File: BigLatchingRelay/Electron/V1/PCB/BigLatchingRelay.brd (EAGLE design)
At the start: 89.5 x 29.3 mm, 13 parts, among them IC2 BD6211F

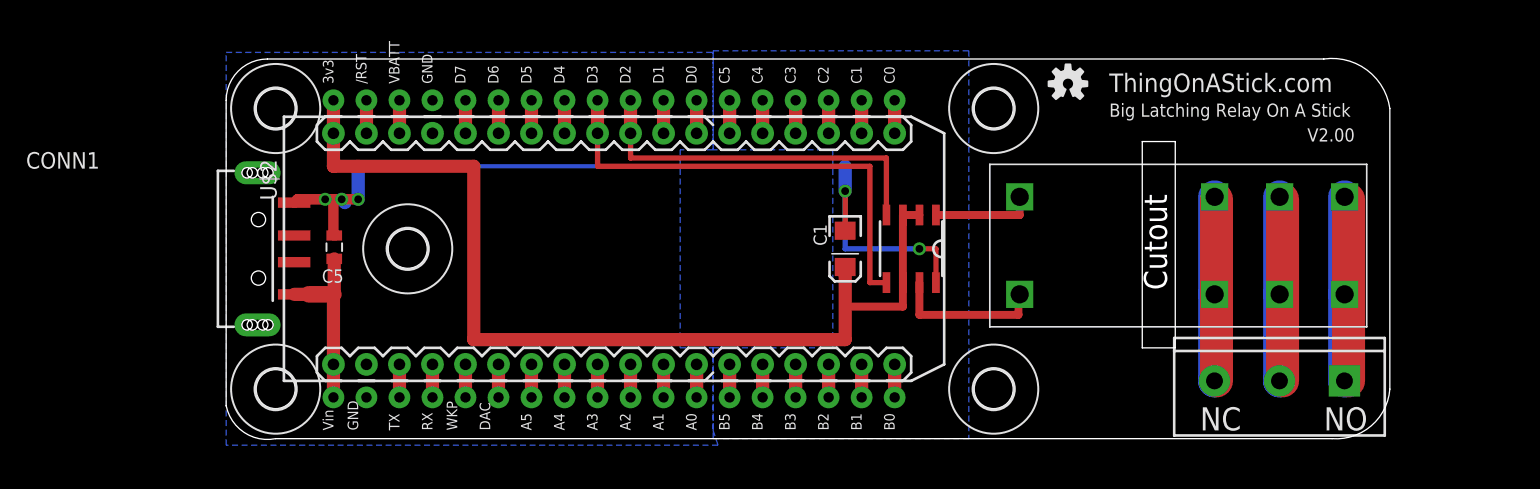
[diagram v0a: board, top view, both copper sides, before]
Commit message: Renamed BigLatchingRelay. Updated to V2.1: Moved connector to end rather than side to reduce strain on one side when USB A connector used. Added OSH Logo LED (and bigger OSH Logo). Added high volage warning text to board top and bottom. Added PDFs of board and schematic.
Added DirtyPcb images.
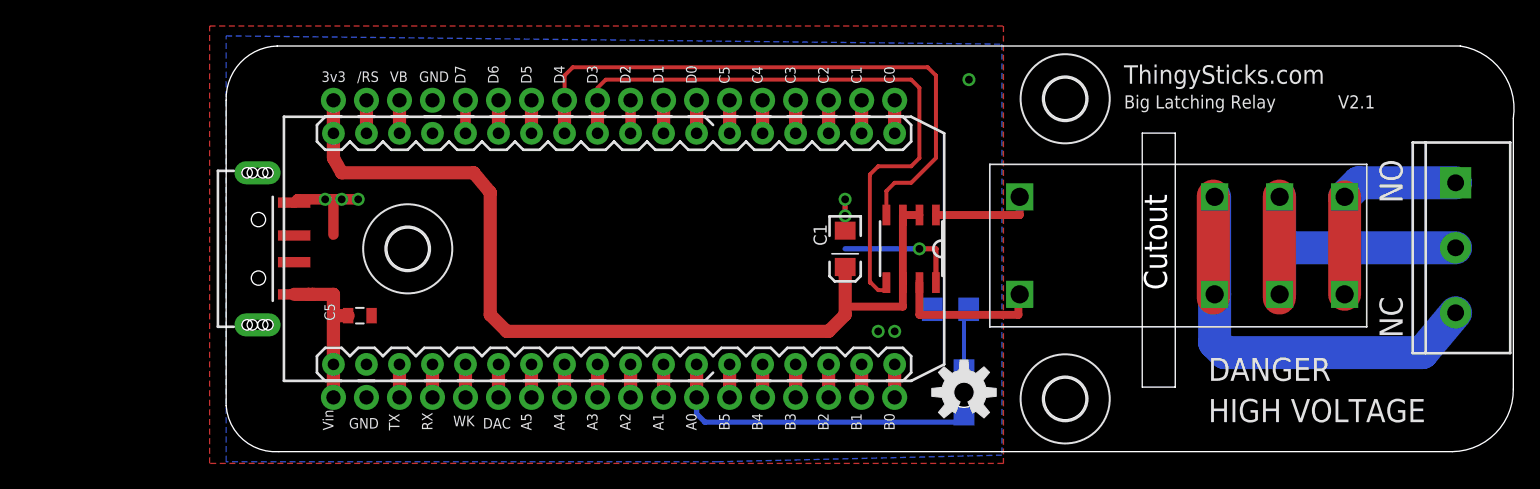
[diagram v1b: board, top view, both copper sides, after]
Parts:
- removed H4, H5: MOUNT-HOLE3.0, holes:3,0
- removed LOGO2: OSHW-LOGOS, SparkFun-Aesthetics:OSHW-LOGO-S
- added D1: (no value), SparkFun-LED:LED-1206-BOTTOM
- added LOGO1: OSHW-LOGOM, SparkFun-Aesthetics:OSHW-LOGO-M
- added R1: (no value), SparkFun-Resistors:1206
- H1, H2, H3: value MOUNT-HOLE3.0 -> MOUNT-HOLE3.2; device holes:3,0 -> holes:3,2
- moved JP1 17.5 mm to (109.8, 17.8), turned to 270 degrees
- moved C5 5.63 mm to (25.5, 7.56), turned to 180 degrees
- moved H2 5.55 mm to (79.8, 24.2)
- moved H3 5.55 mm to (79.8, 1.16)
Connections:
- removed net N$39 (its old number): U$2.A0, U$2.A0_1
- new net N$11: D1.C, R1.2
- new net OSHLED: D1.A, U$2.A0, U$2.A0_1
- net GND: now also R1.1
- net N$20: now also U$2.D2, U$2.D2_1; no longer U$2.D4, U$2.D4_1
- net RELAY1_FORWARD: now also U$2.D4, U$2.D4_1; no longer U$2.D2, U$2.D2_1
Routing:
- net GND: track 67.2 -> 19.7 mm, vias 5 -> 9
- net OSHLED: track 0.00 -> 24.9 mm
- net RELAY1_FORWARD: track 28.5 -> 46.6 mm
- net N$4: track 14.2 -> 31.5 mm
- net N$30: track 14.0 -> 0.00 mm
- net RELAY1_REVERSE: track 36.3 -> 48.9 mm
- net N$1: track 14.2 -> 21.0 mm
- net N$27: track 14.0 -> 7.85 mm
- net N$19: track 14.0 -> 7.85 mm
- net N$11: track 0.00 -> 4.80 mm
- net 3.3V: track 79.2 -> 75.1 mm
- net N$39 (its old number): track 2.54 -> 0.00 mm
- net N$3: track 14.2 -> 16.5 mm
- net 5V: track 14.2 -> 12.2 mm
- added copper zone on layer 1, net GND
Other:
- board size 89.5 x 29.3 mm -> 99.1 x 31.2 mm
- board text added: "Big Latching Relay"
- board text added: "DANGER"
- board text added: "HIGH VOLTAGE"
- board text added: "ThingySticks.com"
- board text added: "V2.1"
- board text removed: "Big Latching Relay On A Stick"
- board text removed: "ThingOnAStick.com"
- board text removed: "V2.00"
